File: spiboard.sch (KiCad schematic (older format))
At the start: 11 parts, among them P1 CONN_01X02, P2 CONN_01X02, P3 CONN_02X20, SW1 DPST 6A

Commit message: Improve switch footprints, add beveled 3D model.
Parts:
- SW1: footprint Wire_Pads:SolderWirePad_4xSquare_0-8mmDrill -> rpihw:Hack_S201
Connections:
- net at P1.1 (P1): now also SW1.3; no longer SW1.4
- net at P2.1 (P1): now also SW1.1; no longer SW1.2
- net at F1.2: now also SW1.4; no longer SW1.3
- net at F2.2: now also SW1.2; no longer SW1.1
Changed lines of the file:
@@
 F 0 "SW1" H 8050 3050 50  0000 C CNN
 F 1 "DPST 6A" H 8050 2400 50  0000 C CNN
-F 2 "Wire_Pads:SolderWirePad_4xSquare_0-8mmDrill" H 8050 2700 50  0001 C CNN
+F 2 "rpihw:Hack_S201" H 8050 2700 50  0001 C CNN
 F 3 "https://www.ckswitches.com/media/1433/s.pdf" H 8050 2700 50  0001 C CNN
 F 4 "CKN9891-ND" H 8050 2700 60  0001 C CNN "Digi-Key_PN"
@@
 F 6 "C&K" H 8050 2700 60  0001 C CNN "Manufacturer"
 	1    8050 2700
-	1    0    0    -1
+	-1   0    0    -1
 $EndComp
 Wire Wire Line

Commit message: Improve footprints, add 3D model for big TVS diode.
Whoops, I didn't checkin the earlier revision switch footprints, those
revisions will be broken unfortunately.
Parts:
- D2: footprint Diodes_ThroughHole:Diode_DO-201AD_Horizontal_RM15 -> rpihw:Diode_R-6_Horizontal_Unpol_RM15
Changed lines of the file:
@@
 F 0 "D2" H 6850 3350 50  0000 C CNN
 F 1 "33V 53.3V" H 6850 3050 50  0000 C CNN
-F 2 "Diodes_ThroughHole:Diode_DO-201AD_Horizontal_RM15" H 6850 3200 50  0001 C CNN
+F 2 "rpihw:Diode_R-6_Horizontal_Unpol_RM15" H 6850 3200 50  0001 C CNN
 F 3 "https://www.mccsemi.com/pdf/Products/5KP5.0(C)%20~5KP110(C)A%20(R-6).pdf" H 6850 3200 50  0001 C CNN
 F 4 "5KP33CA-TPMSCT-ND" H 6850 3200 60  0001 C CNN "Digi-Key_PN"

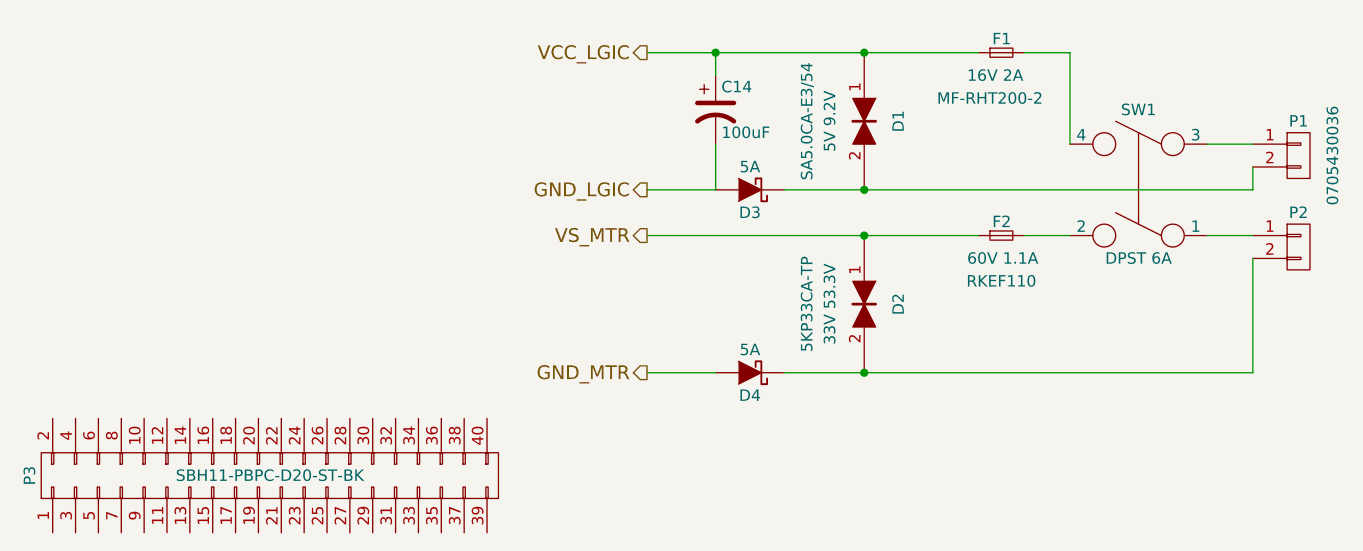
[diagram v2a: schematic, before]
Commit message: Use thermistor schematic for PTC resettable fuse.
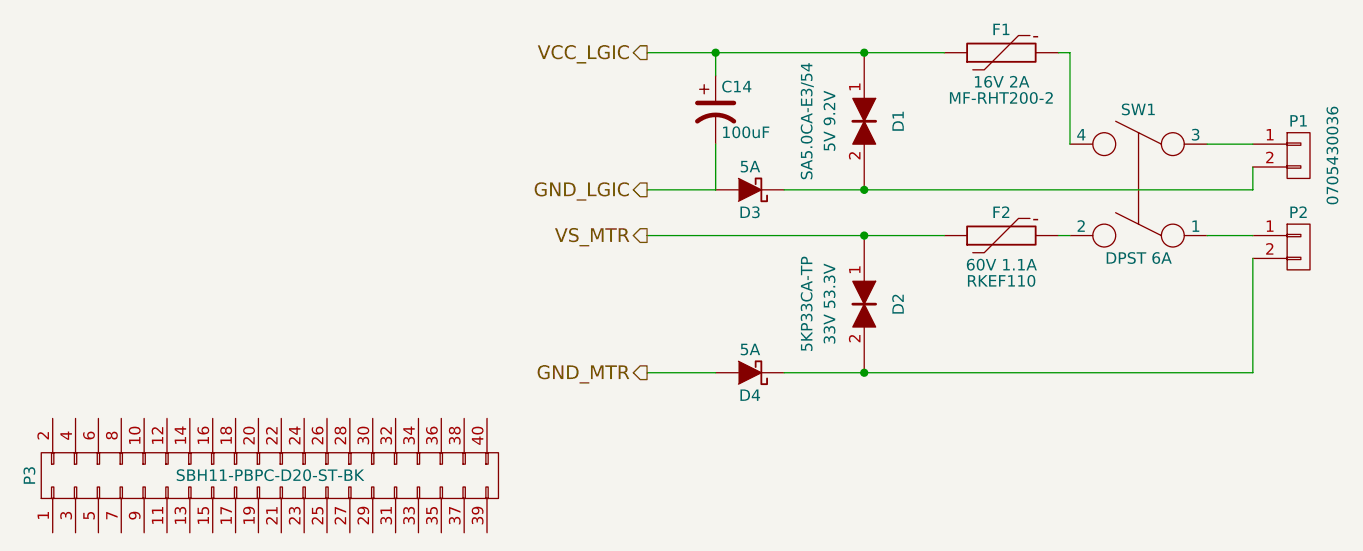
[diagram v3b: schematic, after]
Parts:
- removed F1: 16V 2A, Capacitors_ThroughHole:C_Radial_D5_L11_P2.5, symbol F_Small
- removed F2: 60V 1.1A, Capacitors_ThroughHole:C_Radial_D5_L11_P2.5, symbol F_Small
- added F1: 16V 2A, Capacitors_ThroughHole:C_Radial_D5_L11_P2.5, symbol THERMISTOR
- added F2: 60V 1.1A, Capacitors_ThroughHole:C_Radial_D5_L11_P2.5, symbol THERMISTOR
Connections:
- net VCC_LGIC: now also F1.1
- net VS_MTR: now also F2.1
- net at SW1.4: now also F1.2
- net at SW1.2: now also F2.2
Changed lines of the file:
@@
-	1    0    0    -1
-$EndComp
-$Comp
-L F_Small F1
-U 1 1 5F0663AF
-P 7450 2100
-F 0 "F1" H 7410 2160 50  0000 L CNN
-F 1 "16V 2A" H 7300 2000 50  0000 L CNN
-F 2 "Capacitors_ThroughHole:C_Radial_D5_L11_P2.5" H 7450 2100 50  0001 C CNN
-F 3 "https://www.bourns.com/docs/product-datasheets/mfrht.pdf" H 7450 2100 50  0001 C CNN
-F 4 "MF-RHT200-2CT-ND" H 7450 2100 60  0001 C CNN "Digi-Key_PN"
-F 5 "MF-RHT200-2" H 7400 1900 50  0000 C CNN "MPN"
-F 6 "Bourns Inc." H 7450 2100 60  0001 C CNN "Manufacturer"
-	1    7450 2100
-	1    0    0    -1
-$EndComp
-$Comp
-L F_Small F2
-U 1 1 5F0663E0
-P 7450 2900
-F 0 "F2" H 7410 2960 50  0000 L CNN
-F 1 "60V 1.1A" H 7300 2800 50  0000 L CNN
-F 2 "Capacitors_ThroughHole:C_Radial_D5_L11_P2.5" H 7450 2900 50  0001 C CNN
-F 3 "https://www.littelfuse.com/~/media/electronics/product_specifications/resettable_ptcs/littelfuse_ptc_rkef110_product_specification.pdf.pdf" H 7450 2900 50  0001 C CNN
-F 4 "RKEF110HF-ND" H 7450 2900 60  0001 C CNN "Digi-Key_PN"
-F 5 "RKEF110" H 7450 2700 50  0000 C CNN "MPN"
-F 6 "Littelfuse Inc." H 7450 2900 60  0001 C CNN "Manufacturer"
-	1    7450 2900
 	1    0    0    -1
 $EndComp
 Wire Wire Line
-	5900 2100 7350 2100
+	5900 2100 7200 2100
 Wire Wire Line
-	5900 2900 7350 2900
+	5900 2900 7200 2900
 Wire Wire Line
 	6500 3500 8550 3500
@@
 $EndComp
 Wire Wire Line
-	7550 2900 7750 2900
+	7700 2900 7750 2900
 Wire Wire Line
 	7750 2500 7750 2100
 Wire Wire Line
-	7750 2100 7550 2100
+	7750 2100 7700 2100
 Wire Wire Line
 	8550 2500 8350 2500
+$Comp
+L THERMISTOR F1
+U 1 1 5F8E06AB
+P 7450 2100
+F 0 "F1" V 7550 2100 50  0000 C CNN
+F 1 "16V 2A" V 7350 2100 50  0000 C BNN
+F 2 "Capacitors_ThroughHole:C_Radial_D5_L11_P2.5" H 7450 2100 50  0001 C CNN
+F 3 "https://www.bourns.com/docs/product-datasheets/mfrht.pdf" H 7450 2100 50  0001 C CNN
+F 4 "MF-RHT200-2CT-ND" V 7450 2100 60  0001 C CNN "Digi-Key_PN"
+F 5 "MF-RHT200-2" V 7250 2100 50  0000 C CNN "MPN"
+F 6 "Bourns Inc." V 7450 2100 60  0001 C CNN "Manufacturer"
+	1    7450 2100
+	0    -1   -1   0
+$EndComp
+$Comp
+L THERMISTOR F2
+U 1 1 5F8E0719
+P 7450 2900
+F 0 "F2" V 7550 2900 50  0000 C CNN
+F 1 "60V 1.1A" V 7350 2900 50  0000 C BNN
+F 2 "Capacitors_ThroughHole:C_Radial_D5_L11_P2.5" H 7450 2900 50  0001 C CNN
+F 3 "https://www.littelfuse.com/~/media/electronics/product_specifications/resettable_ptcs/littelfuse_ptc_rkef110_product_specification.pdf.pdf" H 7450 2900 50  0001 C CNN
+F 4 "RKEF110HF-ND" V 7450 2900 60  0001 C CNN "Digi-Key_PN"
+F 5 "RKEF110" V 7250 2900 50  0000 C CNN "MPN"
+F 6 "Littelfuse Inc." V 7450 2900 60  0001 C CNN "Manufacturer"
+	1    7450 2900
+	0    -1   -1   0
+$EndComp
 $EndSCHEMATC
